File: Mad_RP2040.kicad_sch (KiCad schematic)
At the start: 16 parts, among them J1 USB_C_Receptacle, SW12 SW_SPST, SW13 SW_SPST, U0 PCB, U1 ECMF02-2AMX6

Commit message: Move RP2040 controller into local
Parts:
- renumbered D19 to D3, D20 to D4, D21 to D5, D22 to D6, SW12 to SW1, SW13 to SW2, U0 to U2
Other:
- sheet RP2040a renamed RP2040
- sheet RP2040: file mad_lib/schematics/Keyboard Controllers/RP2040.kicad_sch -> Controller_RP2040.kicad_sch
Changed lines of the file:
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@@
 		(on_board yes)
 		(dnp no)
-		(property "Reference" "D21"
+		(property "Reference" "D5"
 			(at 225.425 84.455 0)
 			(effects
@@
 			(project "Mad_RP2040"
 				(path "/eedae293-eb5b-47bd-b383-bccfdf81bf72"
-					(reference "D21")
+					(reference "D5")
 					(unit 1)
 				)
@@
 		(dnp no)
 		(fields_autoplaced yes)
-		(property "Reference" "#PWR05"
+		(property "Reference" "#PWR08"
 			(at 219.075 89.535 0)
 			(effects
@@
 			(project "Mad_RP2040"
 				(path "/eedae293-eb5b-47bd-b383-bccfdf81bf72"
-					(reference "#PWR05")
+					(reference "#PWR08")
 					(unit 1)
 				)
@@
 		(dnp no)
 		(fields_autoplaced yes)
-		(property "Reference" "SW12"
+		(property "Reference" "SW1"
 			(at 232.41 55.245 0)
 			(effects
@@
 			(project "Mad_RP2040"
 				(path "/eedae293-eb5b-47bd-b383-bccfdf81bf72"
-					(reference "SW12")
+					(reference "SW1")
 					(unit 1)
 				)
@@
 		(dnp no)
 		(fields_autoplaced yes)
-		(property "Reference" "#PWR07"
+		(property "Reference" "#PWR05"
 			(at 149.86 62.23 0)
 			(effects
@@
 			(project "Mad_RP2040"
 				(path "/eedae293-eb5b-47bd-b383-bccfdf81bf72"
-					(reference "#PWR07")
+					(reference "#PWR05")
 					(unit 1)
 				)
@@
 		(on_board yes)
 		(dnp no)
-		(property "Reference" "D22"
+		(property "Reference" "D6"
 			(at 225.425 103.505 0)
 			(effects
@@
 			(project "Mad_RP2040"
 				(path "/eedae293-eb5b-47bd-b383-bccfdf81bf72"
-					(reference "D22")
+					(reference "D6")
 					(unit 1)
 				)
@@
 		(dnp no)
 		(fields_autoplaced yes)
-		(property "Reference" "D19"
+		(property "Reference" "D3"
 			(at 223.52 55.245 0)
 			(effects
@@
 			(project "Mad_RP2040"
 				(path "/eedae293-eb5b-47bd-b383-bccfdf81bf72"
-					(reference "D19")
+					(reference "D3")
 					(unit 1)
 				)
@@
 		(dnp no)
 		(fields_autoplaced yes)
-		(property "Reference" "SW13"
+		(property "Reference" "SW2"
 			(at 233.045 67.945 0)
 			(effects
@@
 			(project "Mad_RP2040"
 				(path "/eedae293-eb5b-47bd-b383-bccfdf81bf72"
-					(reference "SW13")
+					(reference "SW2")
 					(unit 1)
 				)
@@
 		(dnp no)
 		(fields_autoplaced yes)
-		(property "Reference" "D20"
+		(property "Reference" "D4"
 			(at 224.155 67.945 0)
 			(effects
@@
 			(project "Mad_RP2040"
 				(path "/eedae293-eb5b-47bd-b383-bccfdf81bf72"
-					(reference "D20")
+					(reference "D4")
 					(unit 1)
 				)
@@
 		(on_board yes)
 		(dnp no)
-		(property "Reference" "U0"
+		(property "Reference" "U2"
 			(at 171.45 190.4999 0)
 			(effects
@@
 			(project "Mad_RP2040"
 				(path "/eedae293-eb5b-47bd-b383-bccfdf81bf72"
-					(reference "U0")
+					(reference "U2")
 					(unit 1)
 				)
@@
 		(on_board yes)
 		(dnp no)
-		(property "Reference" "#PWR010"
+		(property "Reference" "#PWR011"
 			(at 239.395 118.11 0)
 			(effects
@@
 			(project "Mad_RP2040"
 				(path "/eedae293-eb5b-47bd-b383-bccfdf81bf72"
-					(reference "#PWR010")
+					(reference "#PWR011")
 					(unit 1)
 				)
@@
 		(on_board yes)
 		(dnp no)
-		(property "Reference" "#PWR09"
+		(property "Reference" "#PWR07"
 			(at 150.495 114.935 0)
 			(effects
@@
 			(project "Mad_RP2040"
 				(path "/eedae293-eb5b-47bd-b383-bccfdf81bf72"
-					(reference "#PWR09")
+					(reference "#PWR07")
 					(unit 1)
 				)
@@
 		(on_board yes)
 		(dnp no)
-		(property "Reference" "#PWR011"
+		(property "Reference" "#PWR010"
 			(at 239.395 99.06 0)
 			(effects
@@
 			(project "Mad_RP2040"
 				(path "/eedae293-eb5b-47bd-b383-bccfdf81bf72"
-					(reference "#PWR011")
+					(reference "#PWR010")
 					(unit 1)
 				)
@@
 		(dnp no)
 		(fields_autoplaced yes)
-		(property "Reference" "#PWR08"
+		(property "Reference" "#PWR09"
 			(at 219.075 108.585 0)
 			(effects
@@
 			(project "Mad_RP2040"
 				(path "/eedae293-eb5b-47bd-b383-bccfdf81bf72"
-					(reference "#PWR08")
+					(reference "#PWR09")
 					(unit 1)
 				)
@@
 			(color 0 0 0 0.0000)
 		)
-		(property "Sheetname" "RP2040a"
+		(property "Sheetname" "RP2040"
 			(at 153.67 57.7084 0)
 			(effects
@@
 			)
 		)
-		(property "Sheetfile" "mad_lib/schematics/Keyboard Controllers/RP2040.kicad_sch"
+		(property "Sheetfile" "Controller_RP2040.kicad_sch"
 			(at 153.67 107.8996 0)
 			(effects

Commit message: Annotation update
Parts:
- renumbered D3 to D1, D4 to D2, D5 to D3, D6 to D4
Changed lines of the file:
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@@
 		(on_board yes)
 		(dnp no)
-		(property "Reference" "D5"
+		(property "Reference" "D3"
 			(at 225.425 84.455 0)
 			(effects
@@
 			(project "Mad_RP2040"
 				(path "/eedae293-eb5b-47bd-b383-bccfdf81bf72"
-					(reference "D5")
+					(reference "D3")
 					(unit 1)
 				)
@@
 		(dnp no)
 		(fields_autoplaced yes)
-		(property "Reference" "#PWR08"
+		(property "Reference" "#PWR07"
 			(at 219.075 89.535 0)
 			(effects
@@
 			(project "Mad_RP2040"
 				(path "/eedae293-eb5b-47bd-b383-bccfdf81bf72"
-					(reference "#PWR08")
+					(reference "#PWR07")
 					(unit 1)
 				)
@@
 		(on_board yes)
 		(dnp no)
-		(property "Reference" "D6"
+		(property "Reference" "D4"
 			(at 225.425 103.505 0)
 			(effects
@@
 			(project "Mad_RP2040"
 				(path "/eedae293-eb5b-47bd-b383-bccfdf81bf72"
-					(reference "D6")
+					(reference "D4")
 					(unit 1)
 				)
@@
 		(dnp no)
 		(fields_autoplaced yes)
-		(property "Reference" "D3"
+		(property "Reference" "D1"
 			(at 223.52 55.245 0)
 			(effects
@@
 			(project "Mad_RP2040"
 				(path "/eedae293-eb5b-47bd-b383-bccfdf81bf72"
-					(reference "D3")
+					(reference "D1")
 					(unit 1)
 				)
@@
 		(dnp no)
 		(fields_autoplaced yes)
-		(property "Reference" "D4"
+		(property "Reference" "D2"
 			(at 224.155 67.945 0)
 			(effects
@@
 			(project "Mad_RP2040"
 				(path "/eedae293-eb5b-47bd-b383-bccfdf81bf72"
-					(reference "D4")
+					(reference "D2")
 					(unit 1)
 				)
@@
 		(on_board yes)
 		(dnp no)
-		(property "Reference" "#PWR011"
+		(property "Reference" "#PWR010"
 			(at 239.395 118.11 0)
 			(effects
@@
 			(project "Mad_RP2040"
 				(path "/eedae293-eb5b-47bd-b383-bccfdf81bf72"
-					(reference "#PWR011")
+					(reference "#PWR010")
 					(unit 1)
 				)
@@
 		(on_board yes)
 		(dnp no)
-		(property "Reference" "#PWR07"
+		(property "Reference" "#PWR06"
 			(at 150.495 114.935 0)
 			(effects
@@
 			(project "Mad_RP2040"
 				(path "/eedae293-eb5b-47bd-b383-bccfdf81bf72"
-					(reference "#PWR07")
+					(reference "#PWR06")
 					(unit 1)
 				)
@@
 		(on_board yes)
 		(dnp no)
-		(property "Reference" "#PWR010"
+		(property "Reference" "#PWR09"
 			(at 239.395 99.06 0)
 			(effects
@@
 			(project "Mad_RP2040"
 				(path "/eedae293-eb5b-47bd-b383-bccfdf81bf72"
-					(reference "#PWR010")
+					(reference "#PWR09")
 					(unit 1)
 				)
@@
 		(dnp no)
 		(fields_autoplaced yes)
-		(property "Reference" "#PWR09"
+		(property "Reference" "#PWR08"
 			(at 219.075 108.585 0)
 			(effects
@@
 			(project "Mad_RP2040"
 				(path "/eedae293-eb5b-47bd-b383-bccfdf81bf72"
-					(reference "#PWR09")
+					(reference "#PWR08")
 					(unit 1)
 				)

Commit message: remove crumbcatcher name from files
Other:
- title: Crumb Catcher -> Mad RP2040
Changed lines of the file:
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@@
 	(paper "A4")
 	(title_block
-		(title "Crumb Catcher")
+		(title "Mad RP2040")
 		(date "2023-10-25")
 		(rev "A")

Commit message: Add todo
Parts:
- renumbered U2 to U0
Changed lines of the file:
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@@
+		)
+	)
+	(text_box "TODO:\n\n* Cleanup bom, remove trailing spaces\n* Get missing 3D models\n* Finish off PCB routing\n* Check LED selection\n* BOM consolidation if possible\n* Create template for page title block"
+		(exclude_from_sim no)
+		(at 151.765 -34.925 0)
+		(size 132.715 45.72)
+		(stroke
+			(width 0)
+			(type default)
+		)
+		(fill
+			(type none)
+		)
+		(effects
+			(font
+				(size 3 3)
+				(thickness 0.6)
+				(bold yes)
+			)
+			(justify left top)
 		)
 	)
@@
 		(on_board yes)
 		(dnp no)
-		(property "Reference" "U2"
+		(property "Reference" "U0"
 			(at 171.45 190.4999 0)
 			(effects
@@
 			(project "Mad_RP2040"
 				(path "/eedae293-eb5b-47bd-b383-bccfdf81bf72"
-					(reference "U2")
+					(reference "U0")
 					(unit 1)
 				)

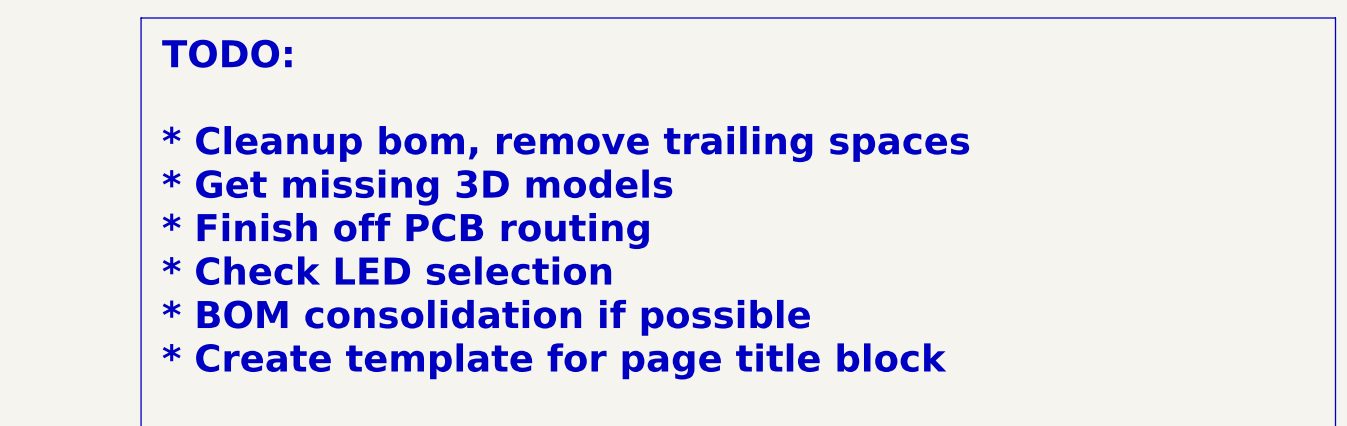
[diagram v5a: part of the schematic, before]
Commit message: Cleanup bom, remove spaces and lcsc fields
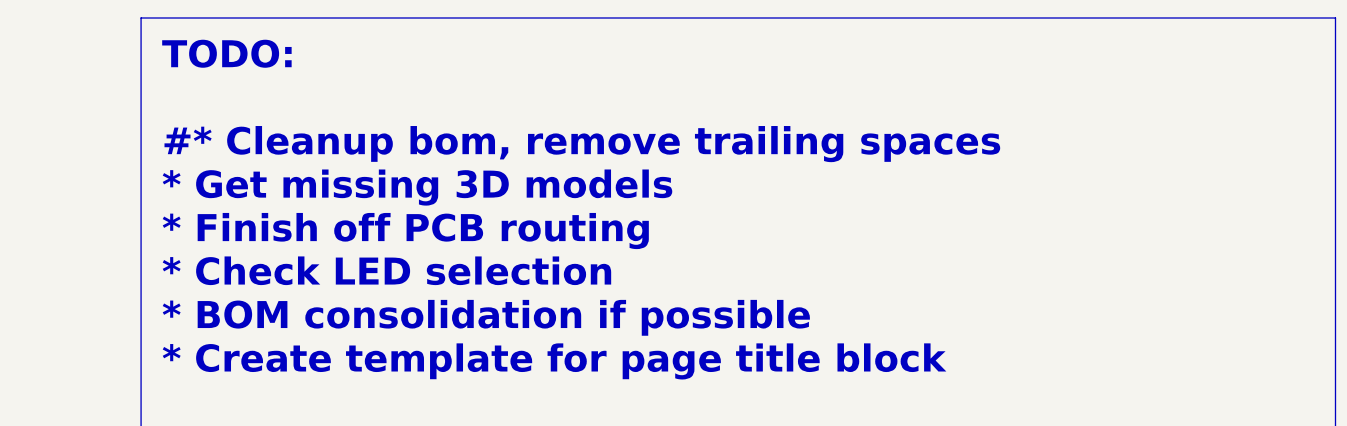
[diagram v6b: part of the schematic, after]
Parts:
- D1, D2: Price $0.18 -> $0.18
- D3: JLC Basic N -> (none); LCSC C965556 -> (none); MPN  SK6812_MINI_E -> (none); Manufacturer Worldsemi -> Worldsemi; Substitute N -> (none)
- D4: JLC Basic N -> (none); LCSC C965556 -> (none); MPN  WS2812C-2020 -> (none); Manufacturer Worldsemi -> Worldsemi; Substitute N -> (none)
- J1: Price $1.29 -> $1.29
- R1, R2: Price $0.16 -> $0.16
- U1: Price $0.83 -> $0.83

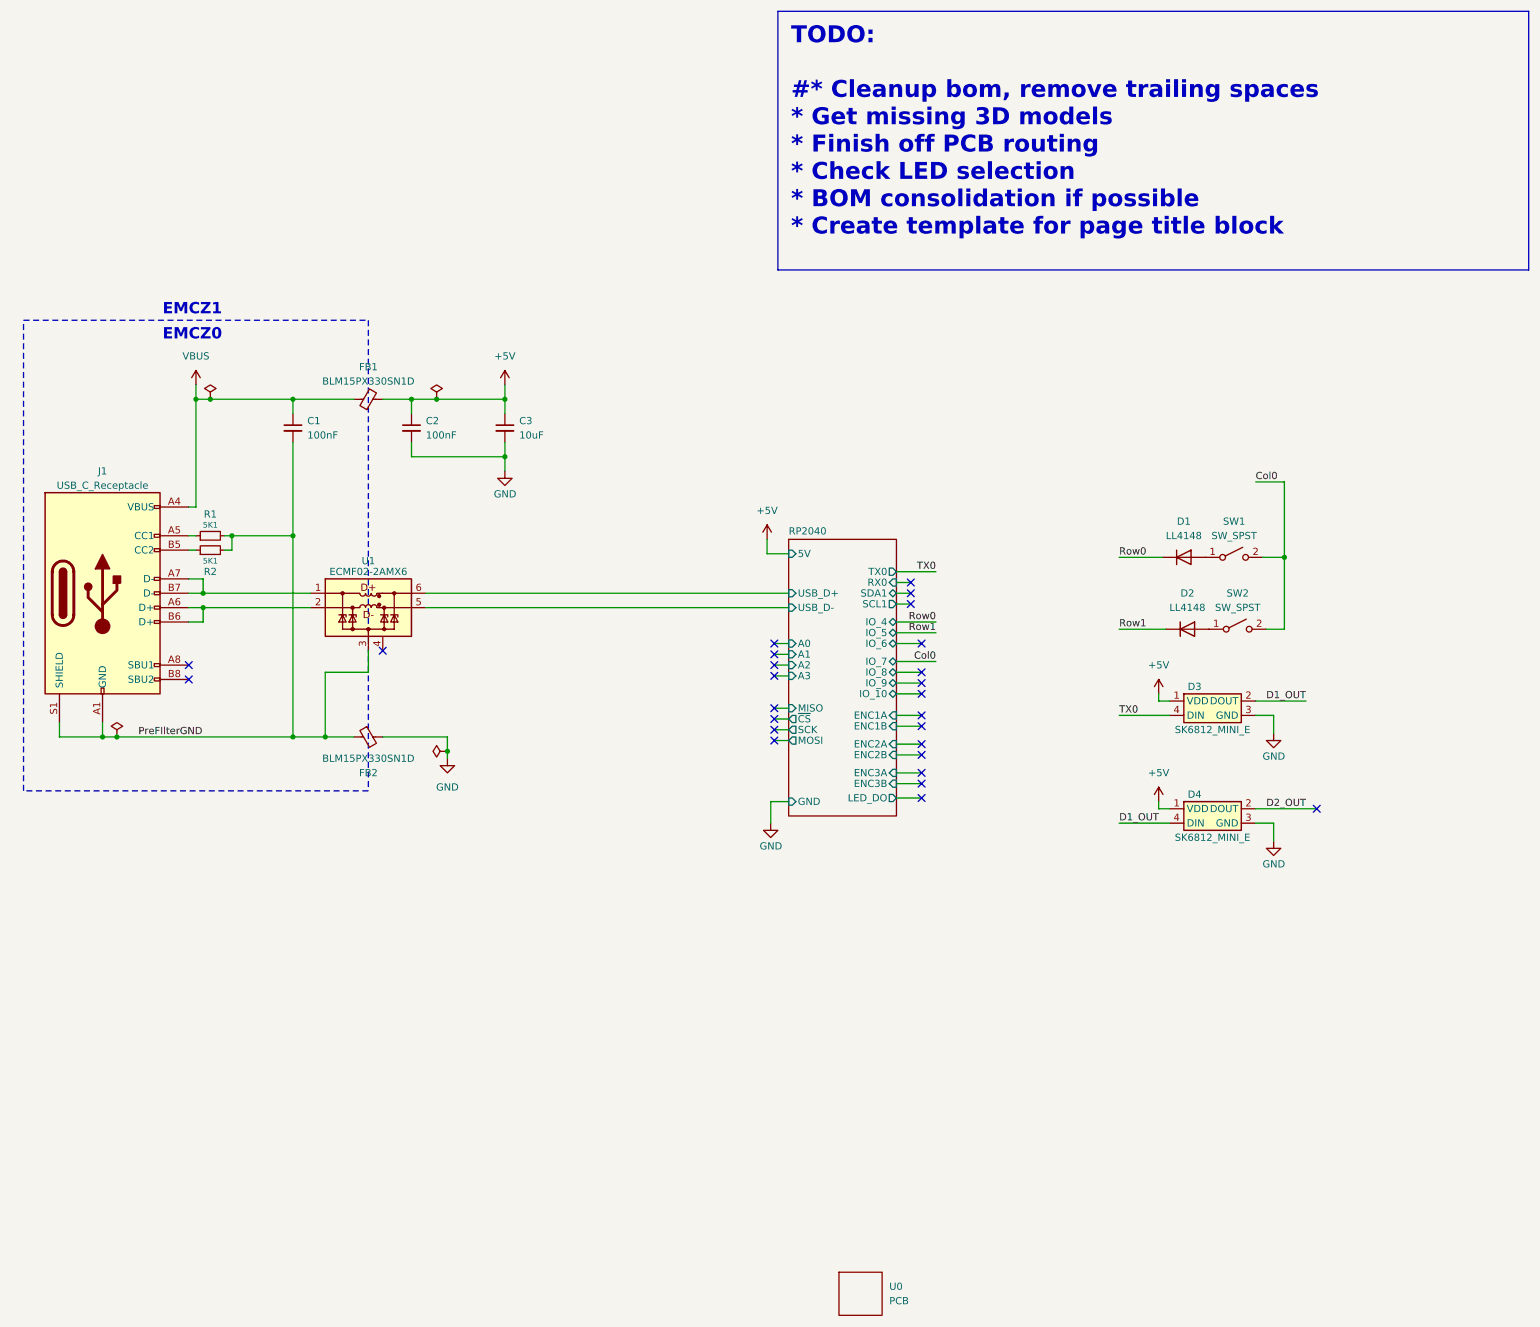
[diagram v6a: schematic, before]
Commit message: Update Models, Finalize LED selections, add backlight, ...
 add mounting holes, add fids, cleanup
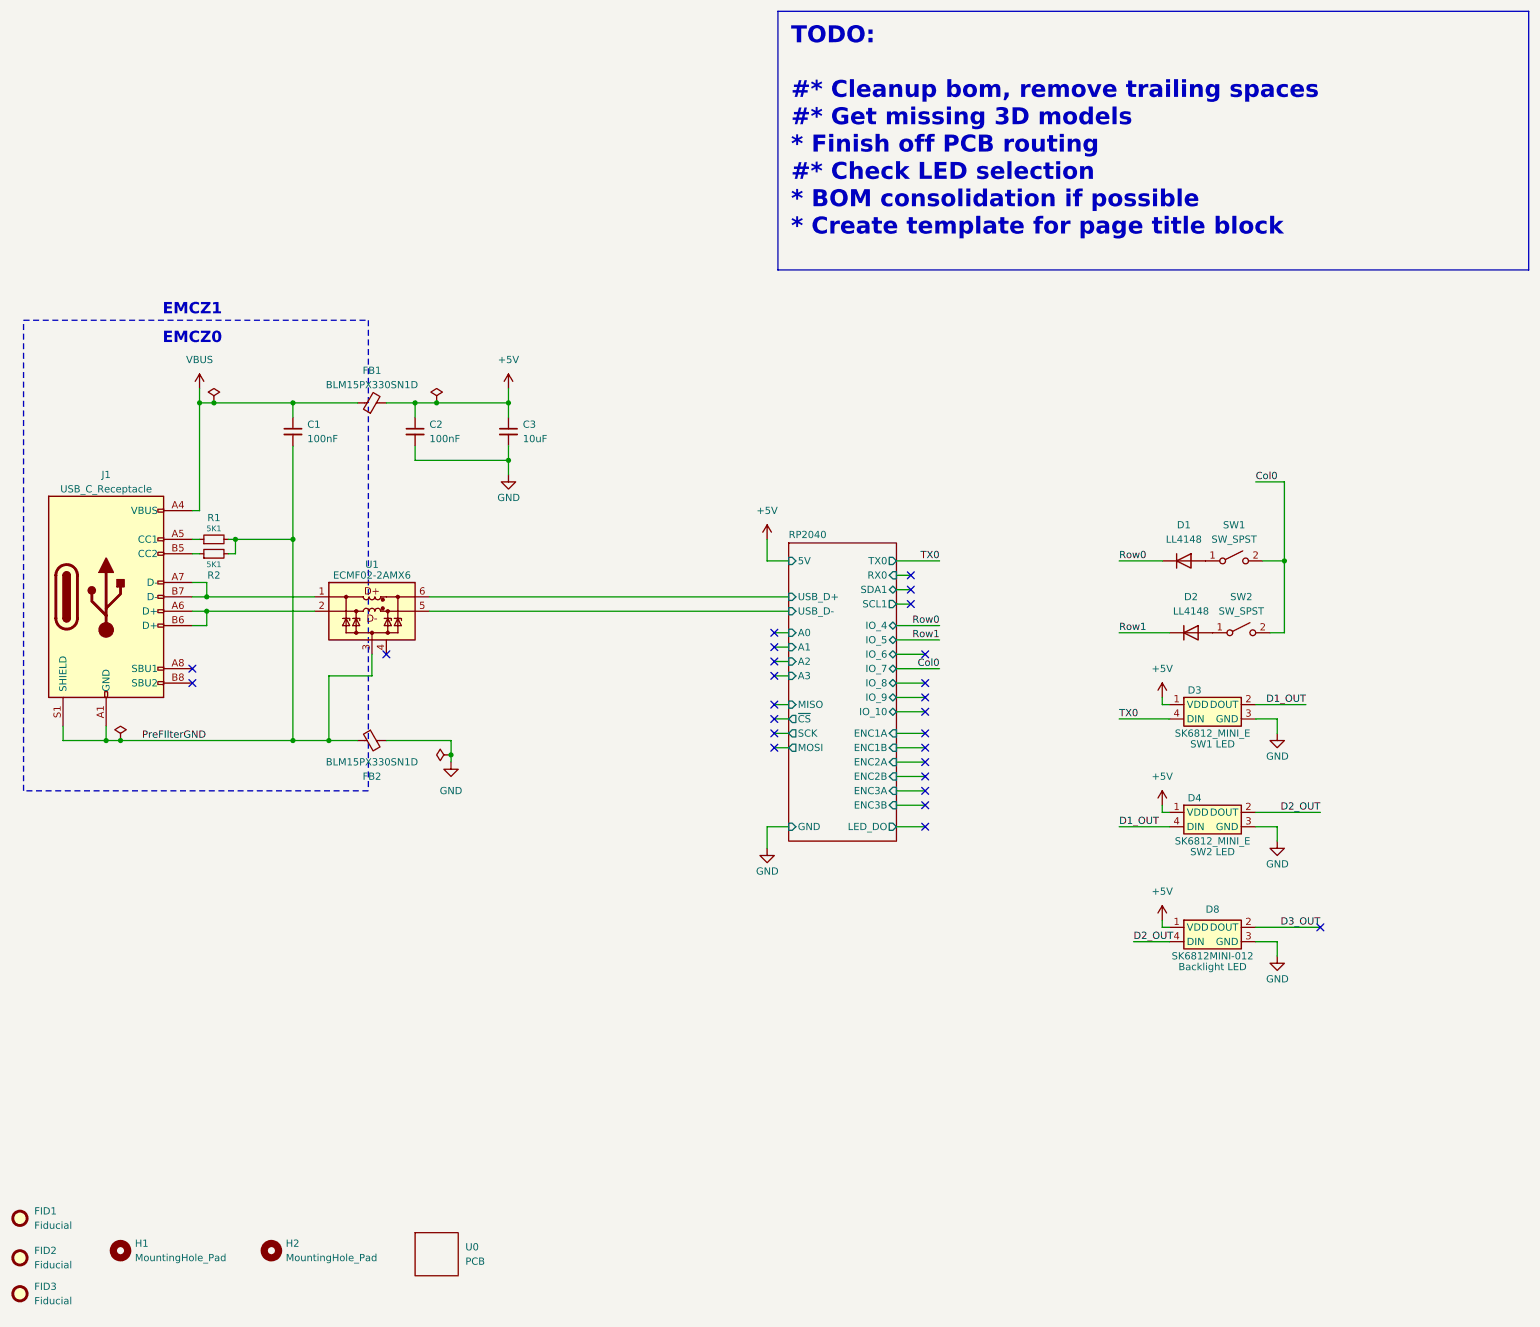
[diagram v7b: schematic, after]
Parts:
- added D8: SK6812MINI-012, Mad_Footprints:SK6812MINI-012, symbol Mad_Symbols:SK6812MINI-012
- added FID1, FID2, FID3: Fiducial, Fiducial:Fiducial_1mm_Mask2mm, symbol Mechanical:Fiducial
- added H1, H2: MountingHole_Pad, MountingHole:MountingHole_2.2mm_M2_DIN965, symbol Mechanical:MountingHole
- D3: footprint Mad_Footprints:SK6812_mini_e -> Mad_Footprints:SK6812MINI-E; symbol Mad_Symbols:SK6812_Mini_E -> Mad_Symbols:SK6812MINI-E; Interface (none) -> SW1 LED; Rating 3.7...5.3V -> 3.7-5.3V (0.2W); Supplier PN C5149201 -> C5149201
- D4: footprint Mad_Footprints:SK6812_mini_e -> Mad_Footprints:SK6812MINI-E; symbol Mad_Symbols:SK6812_Mini_E -> Mad_Symbols:SK6812MINI-E; Interface (none) -> SW2 LED; Rating 3.7...5.3V -> 3.7-5.3V (0.2W); Supplier PN C5149201 -> C5149201
- U1: footprint Package_DFN_QFN:ST_UQFN-6L_1.5x1.7mm_P0.5mm -> Mad_Footprints:ST_UQFN-6L_1.5x1.7mm_P0.5mm
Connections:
- net +5V: now also D8.1 (VDD)
- net D2_OUT: now also D8.4 (DIN)
- net GND: now also D8.3 (GND)
- new net D3_OUT: D8.2 (DOUT)
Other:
- company: MadMan -> ${COMPANY}
- title: Mad RP2040 -> ${TITLE}
- moved on the sheet: C1, C2, C3, D1, D2, D3, D4, FB1, FB2, J1, R1, R2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
